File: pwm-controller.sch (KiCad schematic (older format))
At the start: 32 parts, among them J1 POWER, J2 LOW SIDE, J3 CTRL, J4 POWER, J5 LOW SIDE, Q1 AO3400A, Q2 AO3400A, Q3 AO3400A, Q4 AO3400A, Q5 AO3400A, Q6 AO3400A, Q7 AO3400A, U1 L78L12_SOT89, U2 MCP1416

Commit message: ready, but some cost-saving opportunities left
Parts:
- removed C3: 1u/50, Capacitor_SMD:C_0603_1608Metric, symbol Device:C
- removed C4: 100n/50, Capacitor_SMD:C_0402_1005Metric, symbol Device:C
- removed C5: 10n, Capacitor_SMD:C_0402_1005Metric_Pad0.74x0.62mm_HandSolder, symbol Device:C
- removed D1, D2: Schottky, Diode_SMD:D_SMA, symbol Device:D_Schottky
- removed H3, H7: JLC, mark:JLCPCB_ToolingHole_1152_1300_1400_1650, symbol Mechanical:MountingHole
- removed H6, H8: M2, MountingHole:MountingHole_2.2mm_M2, symbol Mechanical:MountingHole
- removed J3: CTRL, Connector_PinHeader_2.54mm:PinHeader_1x02_P2.54mm_Vertical, symbol Connector_Generic:Conn_01x02
- removed Q1, Q2, Q3, Q4, Q5, Q6, Q7: AO3400A, Package_TO_SOT_SMD:SOT-23, symbol Transistor_FET:AO3400A
- removed R1: 4.7k, Resistor_SMD:R_0402_1005Metric, symbol Device:R
- removed R2: 100, Resistor_SMD:R_0603_1608Metric_Pad0.98x0.95mm_HandSolder, symbol Device:R
- removed R3: 4.7k, Resistor_SMD:R_0402_1005Metric_Pad0.72x0.64mm_HandSolder, symbol Device:R
- removed U1: L78L12_SOT89, Package_TO_SOT_SMD:SOT-89-3, symbol Regulator_Linear:L78L12_SOT89
- removed U2: MCP1416, Package_TO_SOT_SMD:SOT-23-5, symbol Driver_FET:MCP1416
- added C21, C22, C23, C6: 3.3n, Capacitor_SMD:C_0402_1005Metric, symbol Device:C
- added C7, C8: 100n/50, Capacitor_SMD:C_0402_1005Metric, symbol Device:C
- added C9: 1u/50, Capacitor_SMD:C_0603_1608Metric, symbol Device:C
- added D1: Green, LED_SMD:LED_0603_1608Metric, symbol Device:LED
- added D2: Blue, LED_SMD:LED_0603_1608Metric, symbol Device:LED
- added J6: DEBUG, Connector_PinHeader_2.54mm:PinHeader_1x05_P2.54mm_Vertical, symbol Connector_Generic:Conn_01x05
- added J7: I2C, Connector_PinHeader_2.54mm:PinHeader_2x05_P2.54mm_Vertical, symbol Connector_Generic:Conn_02x05_Odd_Even
- added R10, R11, R13, R14, R20, R4, R5, R6, R7, R8, R9: 4.7k, Resistor_SMD:R_0402_1005Metric, symbol Device:R
- added R12, R15, R16, R21, R22: 120, Resistor_SMD:R_0402_1005Metric, symbol Device:R
- added SW1: EC12D1524403, mark:RotaryEncoder_Alps_EC12D_Vertical_H20mm_easy, symbol Device:RotaryEncoder_Switch
- added U1: L78L09_SOT89, Package_TO_SOT_SMD:SOT-89-3, symbol Regulator_Linear:L78L09_SOT89
- added U3: STM8S003F3Px, Package_SO:TSSOP-20_4.4x6.5mm_P0.65mm, symbol mcu:STM8S003F3Px
- added U4: HT7533-1-SOT89, Package_TO_SOT_SMD:SOT-89-3, symbol Regulator_Linear:HT75xx-1-SOT89
- J1: value POWER -> IN-; footprint TerminalBlock_Phoenix:TerminalBlock_Phoenix_MKDS-1,5-3-5.08_1x03_P5.08mm_Horizontal -> mark:ScrewTerminal_5.08P_1x02_10.16x10.16mm; symbol Connector:Screw_Terminal_01x03 -> Connector:Screw_Terminal_01x02; JLC C474953 -> C8465
- J2: value LOW SIDE -> OUT-; footprint TerminalBlock_Phoenix:TerminalBlock_Phoenix_MKDS-1,5-3-5.08_1x03_P5.08mm_Horizontal -> mark:ScrewTerminal_5.08P_1x02_10.16x10.16mm; symbol Connector:Screw_Terminal_01x03 -> Connector:Screw_Terminal_01x02; JLC C474953 -> C8465
- J4: value POWER -> IN+; footprint TerminalBlock_Phoenix:TerminalBlock_Phoenix_MKDS-1,5-3-5.08_1x03_P5.08mm_Horizontal -> mark:ScrewTerminal_5.08P_1x02_10.16x10.16mm; symbol Connector:Screw_Terminal_01x03 -> Connector:Screw_Terminal_01x02; JLC C474953 -> C8465
- J5: value LOW SIDE -> OUT+; footprint TerminalBlock_Phoenix:TerminalBlock_Phoenix_MKDS-1,5-3-5.08_1x03_P5.08mm_Horizontal -> mark:ScrewTerminal_5.08P_1x02_10.16x10.16mm; symbol Connector:Screw_Terminal_01x03 -> Connector:Screw_Terminal_01x02; JLC C474953 -> C8465
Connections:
- net labels added: +3.3V, +9V, DRAIN1, DRAIN2, INT, LED1, LED2, PWM1, PWM2, RE_B, RE_I, RE_Q, SADD0, SADD1, SADD2, SCL, SDA, SWIM, URX, UTX, VIN
- net labels removed: 12VIN, 24VIN, CTRL, DRAIN, GATE, GATE_DRV, VDD
- wire segments 48 -> 21
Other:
- note added: "<20mA for control+driver, <10A for target"
- note added: "AN2860 p10f3"
- note added: "Debug and slave interrupt"
- note added: "Digital"
- note added: "I2C and master/slave/address config"
- note added: "INT is I2C interrupt for\nslaves to callback on."
- note added: "Mechanical"
- note added: "Output drivers"
- note added: "Power"
- note added: "Rotary encoder"
- note removed: "GND needs to sink high currents (20A)\n+24/12V sources <1A"
- note removed: "Max 18Vdd"
- moved on the sheet: C1, C2, H1, H2, H4, H5

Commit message: dual channel, cheaper (jellybean gate driver)
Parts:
- removed J1: IN-, mark:ScrewTerminal_5.08P_1x02_10.16x10.16mm, symbol Connector:Screw_Terminal_01x02
- removed R20: 4.7k, Resistor_SMD:R_0402_1005Metric, symbol Device:R
- removed R21, R22: 120, Resistor_SMD:R_0402_1005Metric, symbol Device:R
- added R17: 4.7k, Resistor_SMD:R_0402_1005Metric, symbol Device:R
- J4: value IN+ -> POWER
- J6: JLC - -> C50950
- J7: JLC - -> C492399
- R12: value 120 -> 4.7k; JLC C25079 -> C25900
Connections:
- wire segments 21 -> 18
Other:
- note added: "Vin(max)=30V\nIout(min)=1mA"
- moved on the sheet: J4
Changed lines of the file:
@@
-$Comp
-L Connector:Screw_Terminal_01x02 J?
-U 1 1 61C15452
-P 1050 2350
-AR Path="/61B5C5B6/61C15452" Ref="J?"  Part="1"
-AR Path="/61C15452" Ref="J1"  Part="1"
-F 0 "J1" H 968 2025 50  0000 C CNN
-F 1 "IN-" H 968 2116 50  0000 C CNN
-F 2 "mark:ScrewTerminal_5.08P_1x02_10.16x10.16mm" H 1050 2350 50  0001 C CNN
-F 3 "https://datasheet.lcsc.com/lcsc/1912251636_Ningbo-Kangnex-Elec-WJ500V-5.08-2P_C8465.pdf" H 1050 2350 50  0001 C CNN
-F 4 "C8465" H 1050 2350 50  0001 C CNN "JLC"
-	1    1050 2350
-	-1   0    0    1
-$EndComp
 $Comp
 L Connector:Screw_Terminal_01x02 J?
 U 1 1 61D43916
-P 1750 2250
+P 1050 2400
 AR Path="/61B5C5B6/61D43916" Ref="J?"  Part="1"
 AR Path="/61D43916" Ref="J4"  Part="1"
-F 0 "J4" H 1668 2567 50  0000 C CNN
-F 1 "IN+" H 1668 2476 50  0000 C CNN
-F 2 "mark:ScrewTerminal_5.08P_1x02_10.16x10.16mm" H 1750 2250 50  0001 C CNN
-F 3 "https://datasheet.lcsc.com/lcsc/1912251636_Ningbo-Kangnex-Elec-WJ500V-5.08-2P_C8465.pdf" H 1750 2250 50  0001 C CNN
-F 4 "C8465" H 1750 2250 50  0001 C CNN "JLC"
-	1    1750 2250
-	-1   0    0    -1
+F 0 "J4" H 968 2075 50  0000 C CNN
+F 1 "POWER" H 968 2166 50  0000 C CNN
+F 2 "mark:ScrewTerminal_5.08P_1x02_10.16x10.16mm" H 1050 2400 50  0001 C CNN
+F 3 "https://datasheet.lcsc.com/lcsc/1912251636_Ningbo-Kangnex-Elec-WJ500V-5.08-2P_C8465.pdf" H 1050 2400 50  0001 C CNN
+F 4 "C8465" H 1050 2400 50  0001 C CNN "JLC"
+	1    1050 2400
+	-1   0    0    1
 $EndComp
 $Comp
 L power:GND #PWR0103
 U 1 1 61D4A984
-P 1250 2450
+P 1250 2400
 AR Path="/61D4A984" Ref="#PWR0103"  Part="1"
 AR Path="/61B5C5B6/61D4A984" Ref="#PWR?"  Part="1"
@@
 AR Path="/61C031A1/61D4A984" Ref="#PWR?"  Part="1"
 AR Path="/61C031A3/61D4A984" Ref="#PWR?"  Part="1"
-F 0 "#PWR0103" H 1250 2200 50  0001 C CNN
-F 1 "GND" H 1255 2277 50  0000 C CNN
-F 2 "" H 1250 2450 50  0001 C CNN
-F 3 "" H 1250 2450 50  0001 C CNN
-	1    1250 2450
-	1    0    0    -1
-$EndComp
-Wire Wire Line
-	1250 2450 1250 2350
+F 0 "#PWR0103" H 1250 2150 50  0001 C CNN
+F 1 "GND" H 1255 2227 50  0000 C CNN
+F 2 "" H 1250 2400 50  0001 C CNN
+F 3 "" H 1250 2400 50  0001 C CNN
+	1    1250 2400
+	1    0    0    -1
+$EndComp
 $Comp
 L Connector:Screw_Terminal_01x02 J?
@@
 F 2 "Connector_PinHeader_2.54mm:PinHeader_1x05_P2.54mm_Vertical" H 6350 2400 50  0001 C CNN
 F 3 "~" H 6350 2400 50  0001 C CNN
-F 4 "-" H 6350 2400 50  0001 C CNN "JLC"
+F 4 "C50950" H 6350 2400 50  0001 C CNN "JLC"
 	1    6350 2400
 	-1   0    0    -1
@@
 	1    0    0    -1
 $EndComp
-Wire Wire Line
-	1250 2350 1250 2250
-Connection ~ 1250 2350
-Wire Wire Line
-	1950 2350 1950 2250
 $Comp
 L power:PWR_FLAG #FLG0101
@@
 Wire Wire Line
 	5750 7050 5750 7150
-Wire Wire Line
-	2300 3350 2850 3350
 Text GLabel 8050 3600 2    50   Input ~ 0
 INT
@@
 	1000 3350 1150 3350
 $Comp
-L Device:R R?
-U 1 1 6212DC9D
-P 2850 3500
-AR Path="/61B5C5B6/6212DC9D" Ref="R?"  Part="1"
-AR Path="/61C03040/6212DC9D" Ref="R?"  Part="1"
-AR Path="/61C031A1/6212DC9D" Ref="R?"  Part="1"
-AR Path="/61C031A3/6212DC9D" Ref="R?"  Part="1"
-AR Path="/6212DC9D" Ref="R20"  Part="1"
-F 0 "R20" H 2780 3454 50  0000 R CNN
-F 1 "4.7k" H 2780 3545 50  0000 R CNN
-F 2 "Resistor_SMD:R_0402_1005Metric" V 2780 3500 50  0001 C CNN
-F 3 "~" H 2850 3500 50  0001 C CNN
-F 4 "C25900" H 2850 3500 50  0001 C CNN "JLC"
-	1    2850 3500
-	-1   0    0    1
-$EndComp
-Connection ~ 2850 3350
-Wire Wire Line
-	2850 3350 3100 3350
-$Comp
-L power:GND #PWR?
-U 1 1 6212E365
-P 2850 3650
-AR Path="/61B5C5B6/6212E365" Ref="#PWR?"  Part="1"
-AR Path="/61C03040/6212E365" Ref="#PWR?"  Part="1"
-AR Path="/61C031A1/6212E365" Ref="#PWR?"  Part="1"
-AR Path="/61C031A3/6212E365" Ref="#PWR?"  Part="1"
-AR Path="/6212E365" Ref="#PWR021"  Part="1"
-F 0 "#PWR021" H 2850 3400 50  0001 C CNN
-F 1 "GND" H 2855 3477 50  0000 C CNN
-F 2 "" H 2850 3650 50  0001 C CNN
-F 3 "" H 2850 3650 50  0001 C CNN
-	1    2850 3650
-	1    0    0    -1
-$EndComp
-$Comp
 L Device:C C1
 U 1 1 61BCD012
@@
 F 2 "Connector_PinHeader_2.54mm:PinHeader_2x05_P2.54mm_Vertical" H 6050 3450 50  0001 C CNN
 F 3 "~" H 6050 3450 50  0001 C CNN
-F 4 "-" H 6050 3450 50  0001 C CNN "JLC"
+F 4 "C492399" H 6050 3450 50  0001 C CNN "JLC"
 	1    6050 3450
 	-1   0    0    -1
@@
 	-1   0    0    1
 $EndComp
-Wire Wire Line
-	1950 4550 2450 4550
-$Comp
-L Device:R R?
-U 1 1 62293FAC
-P 2450 4700
-AR Path="/61B5C5B6/62293FAC" Ref="R?"  Part="1"
-AR Path="/61C03040/62293FAC" Ref="R?"  Part="1"
-AR Path="/61C031A1/62293FAC" Ref="R?"  Part="1"
-AR Path="/61C031A3/62293FAC" Ref="R?"  Part="1"
-AR Path="/62293FAC" Ref="R12"  Part="1"
-F 0 "R12" H 2380 4654 50  0000 R CNN
-F 1 "120" H 2380 4745 50  0000 R CNN
-F 2 "Resistor_SMD:R_0402_1005Metric" V 2380 4700 50  0001 C CNN
-F 3 "~" H 2450 4700 50  0001 C CNN
-F 4 "C25079" H 2450 4700 50  0001 C CNN "JLC"
-	1    2450 4700
-	-1   0    0    1
-$EndComp
-Connection ~ 2450 4550
-$Comp
-L Device:R R?
-U 1 1 6229481F
-P 2600 4850
-AR Path="/61B5C5B6/6229481F" Ref="R?"  Part="1"
-AR Path="/61C03040/6229481F" Ref="R?"  Part="1"
-AR Path="/61C031A1/6229481F" Ref="R?"  Part="1"
-AR Path="/61C031A3/6229481F" Ref="R?"  Part="1"
-AR Path="/6229481F" Ref="R21"  Part="1"
-F 0 "R21" V 2715 4850 50  0000 C CNN
-F 1 "120" V 2806 4850 50  0000 C CNN
-F 2 "Resistor_SMD:R_0402_1005Metric" V 2530 4850 50  0001 C CNN
-F 3 "~" H 2600 4850 50  0001 C CNN
-F 4 "C25079" H 2600 4850 50  0001 C CNN "JLC"
-	1    2600 4850
-	0    1    1    0
-$EndComp
-$Comp
-L Device:R R?
-U 1 1 62294A50
-P 2750 5000
-AR Path="/61B5C5B6/62294A50" Ref="R?"  Part="1"
-AR Path="/61C03040/62294A50" Ref="R?"  Part="1"
-AR Path="/61C031A1/62294A50" Ref="R?"  Part="1"
-AR Path="/61C031A3/62294A50" Ref="R?"  Part="1"
-AR Path="/62294A50" Ref="R22"  Part="1"
-F 0 "R22" H 2680 4954 50  0000 R CNN
-F 1 "120" H 2680 5045 50  0000 R CNN
-F 2 "Resistor_SMD:R_0402_1005Metric" V 2680 5000 50  0001 C CNN
-F 3 "~" H 2750 5000 50  0001 C CNN
-F 4 "C25079" H 2750 5000 50  0001 C CNN "JLC"
-	1    2750 5000
-	-1   0    0    1
-$EndComp
-$Comp
-L power:GND #PWR?
-U 1 1 62295AD8
-P 2750 5150
-AR Path="/61B5C5B6/62295AD8" Ref="#PWR?"  Part="1"
-AR Path="/61C03040/62295AD8" Ref="#PWR?"  Part="1"
-AR Path="/61C031A1/62295AD8" Ref="#PWR?"  Part="1"
-AR Path="/61C031A3/62295AD8" Ref="#PWR?"  Part="1"
-AR Path="/62295AD8" Ref="#PWR039"  Part="1"
-F 0 "#PWR039" H 2750 4900 50  0001 C CNN
-F 1 "GND" H 2755 4977 50  0000 C CNN
-F 2 "" H 2750 5150 50  0001 C CNN
-F 3 "" H 2750 5150 50  0001 C CNN
-	1    2750 5150
-	1    0    0    -1
-$EndComp
-Wire Wire Line
-	2450 4550 3150 4550
-Text GLabel 1950 2250 2    50   Input ~ 0
+Text GLabel 1250 2300 2    50   Input ~ 0
 VIN
 Text GLabel 2850 2300 3    50   Input ~ 0
@@
 Text GLabel 1000 4550 0    50   Input ~ 0
 VIN
+Wire Wire Line
+	2300 3350 2900 3350
+Text Notes 1950 4400 0    50   ~ 0
+Vin(max)=30V\nIout(min)=1mA
+Text Notes 2300 3200 0    50   ~ 0
+Vin(max)=30V\nIout(min)=1mA
+Wire Wire Line
+	1950 4550 2600 4550
+$Comp
+L Device:R R?
+U 1 1 61D455E4
+P 2600 4700
+AR Path="/61B5C5B6/61D455E4" Ref="R?"  Part="1"
+AR Path="/61C03040/61D455E4" Ref="R?"  Part="1"
+AR Path="/61C031A1/61D455E4" Ref="R?"  Part="1"
+AR Path="/61C031A3/61D455E4" Ref="R?"  Part="1"
+AR Path="/61D455E4" Ref="R17"  Part="1"
+F 0 "R17" H 2530 4654 50  0000 R CNN
+F 1 "4.7k" H 2530 4745 50  0000 R CNN
+F 2 "Resistor_SMD:R_0402_1005Metric" V 2530 4700 50  0001 C CNN
+F 3 "~" H 2600 4700 50  0001 C CNN
+F 4 "C25900" H 2600 4700 50  0001 C CNN "JLC"
+	1    2600 4700
+	-1   0    0    1
+$EndComp
+Connection ~ 2600 4550
+Wire Wire Line
+	2600 4550 3150 4550
+$Comp
+L power:GND #PWR?
+U 1 1 61D45C13
+P 2600 4850
+AR Path="/61B5C5B6/61D45C13" Ref="#PWR?"  Part="1"
+AR Path="/61C03040/61D45C13" Ref="#PWR?"  Part="1"
+AR Path="/61C031A1/61D45C13" Ref="#PWR?"  Part="1"
+AR Path="/61C031A3/61D45C13" Ref="#PWR?"  Part="1"
+AR Path="/61D45C13" Ref="#PWR028"  Part="1"
+F 0 "#PWR028" H 2600 4600 50  0001 C CNN
+F 1 "GND" V 2605 4722 50  0000 R CNN
+F 2 "" H 2600 4850 50  0001 C CNN
+F 3 "" H 2600 4850 50  0001 C CNN
+	1    2600 4850
+	1    0    0    -1
+$EndComp
+$Comp
+L Device:R R?
+U 1 1 61D46ED7
+P 2900 3500
+AR Path="/61B5C5B6/61D46ED7" Ref="R?"  Part="1"
+AR Path="/61C03040/61D46ED7" Ref="R?"  Part="1"
+AR Path="/61C031A1/61D46ED7" Ref="R?"  Part="1"
+AR Path="/61C031A3/61D46ED7" Ref="R?"  Part="1"
+AR Path="/61D46ED7" Ref="R12"  Part="1"
+F 0 "R12" H 2830 3454 50  0000 R CNN
+F 1 "4.7k" H 2830 3545 50  0000 R CNN
+F 2 "Resistor_SMD:R_0402_1005Metric" V 2830 3500 50  0001 C CNN
+F 3 "~" H 2900 3500 50  0001 C CNN
+F 4 "C25900" H 2900 3500 50  0001 C CNN "JLC"
+	1    2900 3500
+	-1   0    0    1
+$EndComp
+$Comp
+L power:GND #PWR?
+U 1 1 61D46EDD
+P 2900 3650
+AR Path="/61B5C5B6/61D46EDD" Ref="#PWR?"  Part="1"
+AR Path="/61C03040/61D46EDD" Ref="#PWR?"  Part="1"
+AR Path="/61C031A1/61D46EDD" Ref="#PWR?"  Part="1"
+AR Path="/61C031A3/61D46EDD" Ref="#PWR?"  Part="1"
+AR Path="/61D46EDD" Ref="#PWR027"  Part="1"
+F 0 "#PWR027" H 2900 3400 50  0001 C CNN
+F 1 "GND" V 2905 3522 50  0000 R CNN
+F 2 "" H 2900 3650 50  0001 C CNN
+F 3 "" H 2900 3650 50  0001 C CNN
+	1    2900 3650
+	1    0    0    -1
+$EndComp
+Connection ~ 2900 3350
+Wire Wire Line
+	2900 3350 3100 3350
 $EndSCHEMATC

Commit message: ready?
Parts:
- removed C9: 1u/50, Capacitor_SMD:C_0603_1608Metric, symbol Device:C
- removed U1: L78L09_SOT89, Package_TO_SOT_SMD:SOT-89-3, symbol Regulator_Linear:L78L09_SOT89
- removed U4: HT7533-1-SOT89, Package_TO_SOT_SMD:SOT-89-3, symbol Regulator_Linear:HT75xx-1-SOT89
- added R1, R3: 220, Resistor_SMD:R_0402_1005Metric, symbol Device:R
- added TP1: TP5V, TestPoint:TestPoint_Pad_D2.0mm, symbol Connector:TestPoint
- added U1: 78L05, Package_TO_SOT_SMD:SOT-89-3, symbol Regulator_Linear:L78L05_SOT89
- R15, R16: value 120 -> 220; JLC C25079 -> C25091
- R17: value 4.7k -> 220; JLC C25900 -> C25091
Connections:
- net labels added: +5V
- net labels removed: +3.3V, +9V
- wire segments 18 -> 14
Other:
- note added: "Vin(max)=30V\nIout(min)=1mA\nIout(max)=100mA (15mA wrt. thermals)"
- note removed: "Vin(max)=30V\nIout(min)=1mA"
- moved on the sheet: C1, C2, R12

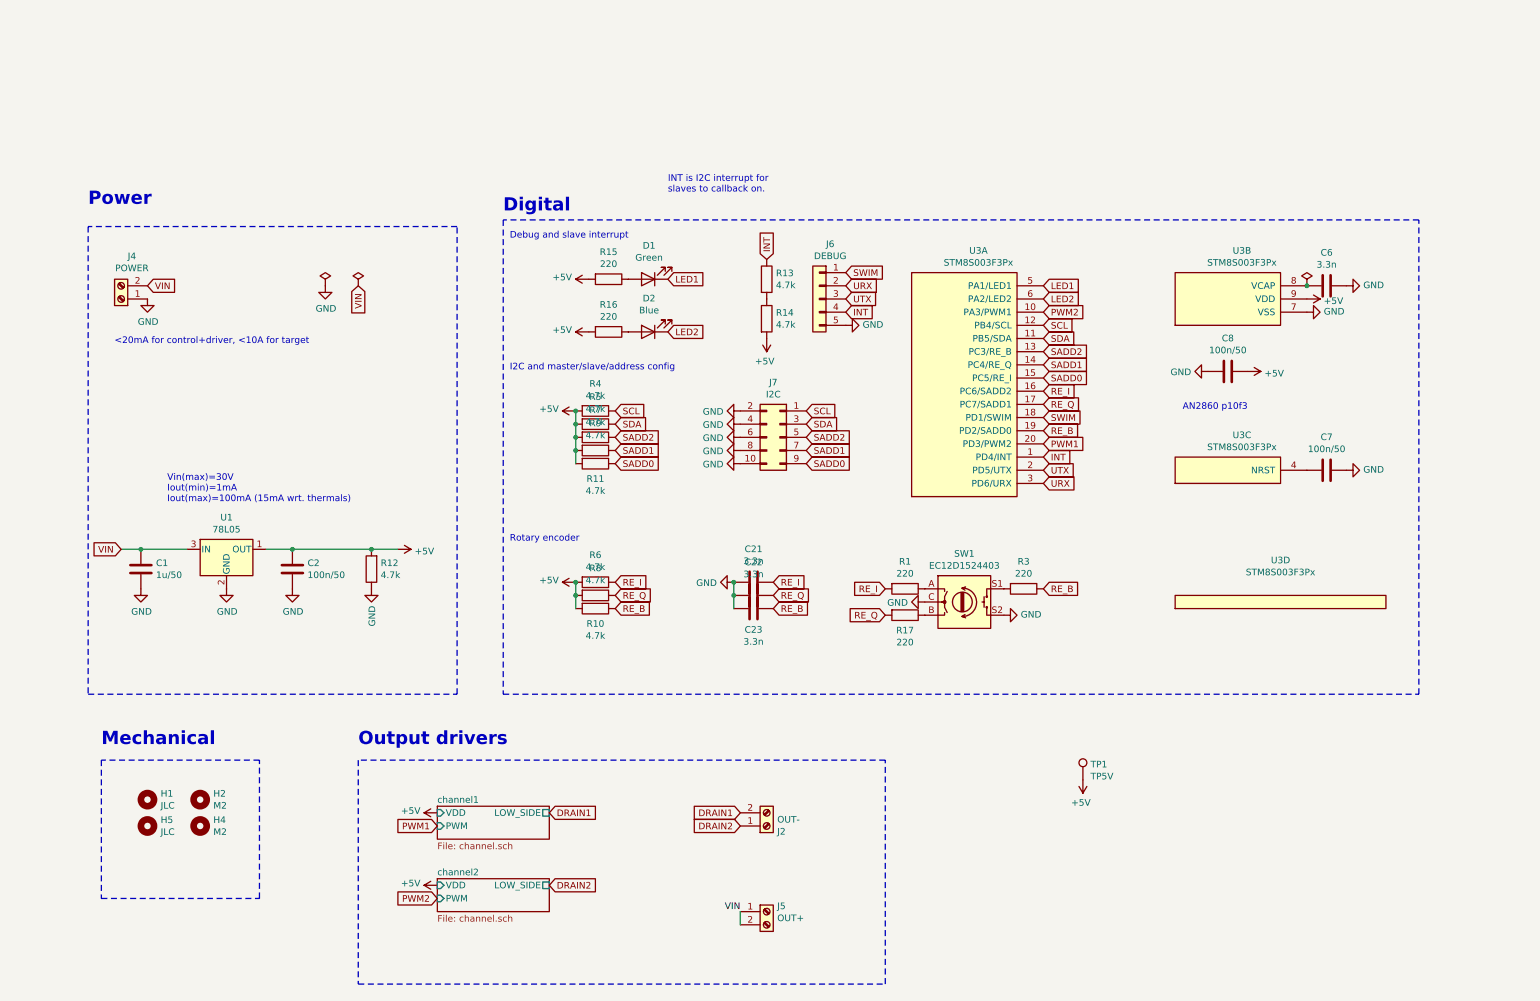
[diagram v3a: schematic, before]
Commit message: about to remove most pullups (use internals instead) and reroute IOs
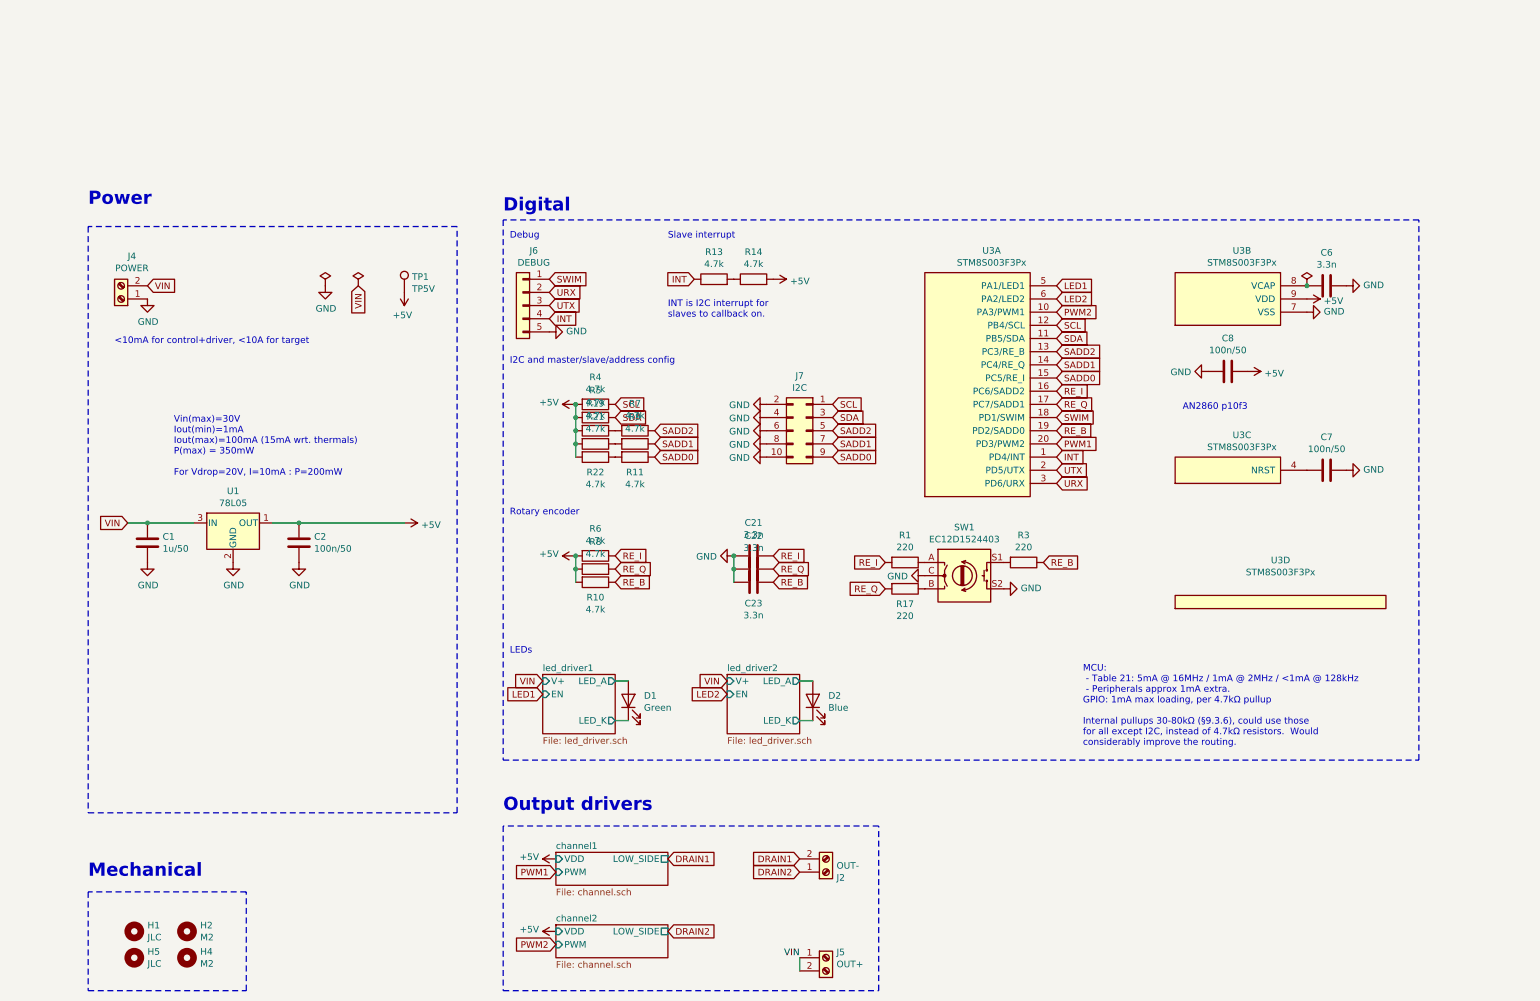
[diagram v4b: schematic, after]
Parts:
- removed R12: 4.7k, Resistor_SMD:R_0402_1005Metric, symbol Device:R
- removed R15, R16: 220, Resistor_SMD:R_0402_1005Metric, symbol Device:R
- added R19, R21, R22: 4.7k, Resistor_SMD:R_0402_1005Metric, symbol Device:R
- TP1: JLC (none) -> -
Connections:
- net +5V: now also R19.2, R21.2, R22.2; no longer R11.2, R7.2, R9.2
- net LED1: no longer D1.1 (K)
- net LED2: no longer D2.1 (K)
- net led_driver1/LED_A: now reaches D1.2 (A)
- net led_driver2/LED_A: now reaches D2.2 (A)
- new net: R19.1, R7.2
- new net: R21.1, R9.2
- new net: R11.2, R22.1
- new net led_driver1/LED_K: D1.1 (K)
- new net led_driver2/LED_K: D2.1 (K)
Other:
- note added: "<10mA for control+driver, <10A for target"
- note added: "Debug"
- note added: "LEDs"
- note added: "MCU:\n - Table 21: 5mA @ 16MHz / 1mA @ 2MHz / <1mA @ 128kHz\n - Peripherals approx 1mA extra.\nGPIO: 1mA max loading, per 4.7kΩ pullup\n\nInternal pullups 30-80kΩ (§9.3.6), could use those\nfor all except I2C, instead of 4.7kΩ resistors. Would\nconsiderably improve the routing."
- note added: "Slave interrupt"
- note added: "Vin(max)=30V\nIout(min)=1mA\nIout(max)=100mA (15mA wrt. thermals)\nP(max) = 350mW\n\nFor Vdrop=20V, I=10mA : P=200mW"
- note removed: "<20mA for control+driver, <10A for target"
- note removed: "Debug and slave interrupt"
- note removed: "Vin(max)=30V\nIout(min)=1mA\nIout(max)=100mA (15mA wrt. thermals)"
- moved on the sheet: C1, C2, C21, C22, C23, D1, D2, H1, H2, H4, H5, J2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
